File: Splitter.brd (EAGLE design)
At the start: 37.8 x 68.5 mm, 46 parts

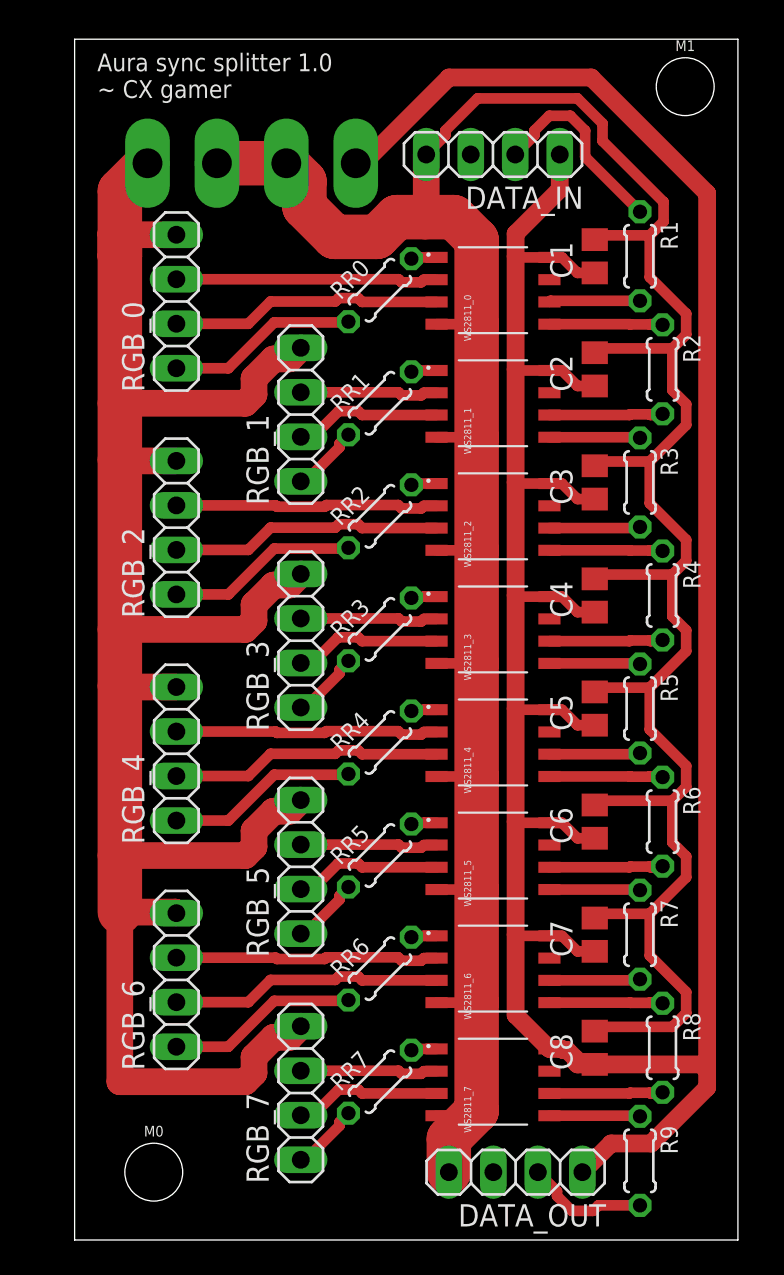
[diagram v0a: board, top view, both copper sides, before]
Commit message: More documentation and upgraded the board to version 1.1
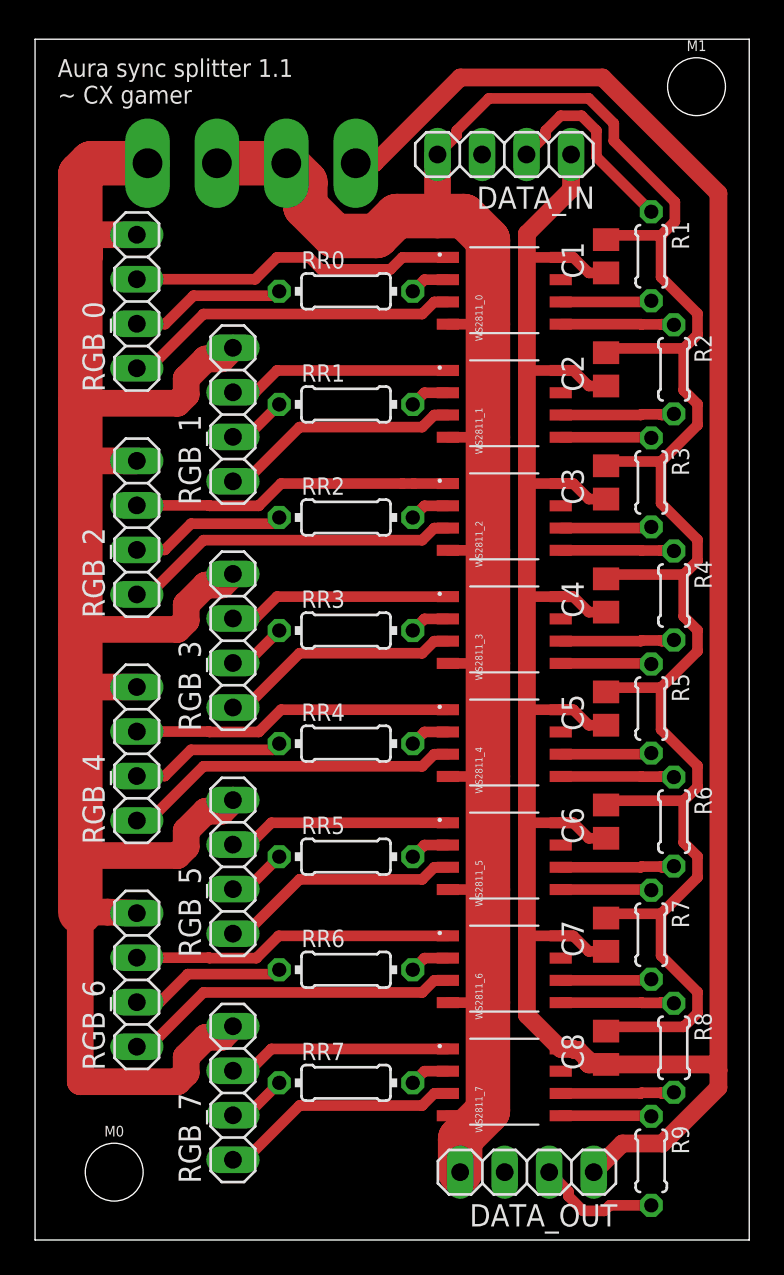
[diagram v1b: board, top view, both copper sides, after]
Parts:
- RR0, RR1, RR2, RR3, RR4, RR5, RR6, RR7: value 30 -> (none); device resistor:0204/5 -> eagle-ltspice:0204/7
- moved RGB_1 3.87 mm to (12.9, 97.4)
- moved RGB_3 3.87 mm to (12.9, 84.5)
- moved RGB_5 3.87 mm to (12.9, 71.6)
- moved RGB_7 3.87 mm to (12.9, 58.7)
- moved RGB_0 2.26 mm to (7.42, 103.9)
- moved RGB_2 2.26 mm to (7.42, 91.0)
- moved RGB_4 2.26 mm to (7.42, 78.1)
- moved RGB_6 2.26 mm to (7.42, 65.2)
- moved M0 2.26 mm to (6.13, 54.2)
- moved RR3 1.94 mm to (19.4, 85.1), turned to 0 degrees
- moved RR4 1.94 mm to (19.4, 78.6), turned to 0 degrees
- moved RR5 1.94 mm to (19.4, 72.2), turned to 0 degrees
- moved RR6 1.94 mm to (19.4, 65.7), turned to 0 degrees
- moved RR0 1.94 mm to (19.4, 104.5), turned to 0 degrees
- moved RR1 1.94 mm to (19.4, 98.0), turned to 0 degrees
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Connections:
- net N$2 renamed S$4
- removed net N$1: RR0.2, WS2811_0.OUTR
- removed net N$11: RR2.2, WS2811_2.OUTR
- removed net N$15: RR3.2, WS2811_3.OUTR
- removed net N$17: RR4.2, WS2811_4.OUTR
- removed net N$19: RR5.2, WS2811_5.OUTR
- removed net N$20: RR6.2, WS2811_6.OUTR
- removed net N$21: RR7.2, WS2811_7.OUTR
- removed net N$24: RGB_5.1, RR5.1
- removed net N$25: RGB_7.2, WS2811_7.OUTB
- removed net N$7: RR1.2, WS2811_1.OUTR
- new net B7: RGB_7.1, WS2811_7.OUTB
- new net R5: RGB_5.2, RR5.1
- new net S$10: RR4.2, WS2811_4.OUTG
- new net S$11: RR5.2, WS2811_5.OUTG
- new net S$13: RR6.2, WS2811_6.OUTG
- new net S$14: RR7.2, WS2811_7.OUTG
- new net S$5: RR0.2, WS2811_0.OUTG
- new net S$6: RR2.2, WS2811_2.OUTG
- new net S$7: RR3.2, WS2811_3.OUTG
- new net S$9: RR1.2, WS2811_1.OUTG
- net B0: now also RGB_0.1; no longer RGB_0.2
- net B1: now also RGB_1.1; no longer RGB_1.2
- net B2: now also RGB_2.1; no longer RGB_2.2
- net B3: now also RGB_3.1; no longer RGB_3.2
- net B4: now also RGB_4.1; no longer RGB_4.2
- net B5: now also RGB_5.1; no longer RGB_5.2
- net B6: now also RGB_6.1; no longer RGB_6.2
- net G0: now also WS2811_0.OUTR; no longer WS2811_0.OUTG
- net G1: now also WS2811_1.OUTR; no longer WS2811_1.OUTG
- net G2: now also WS2811_2.OUTR; no longer WS2811_2.OUTG
- net G3: now also WS2811_3.OUTR; no longer WS2811_3.OUTG
- net G4: now also WS2811_4.OUTR; no longer WS2811_4.OUTG
- net G5: now also WS2811_5.OUTR; no longer WS2811_5.OUTG
- net G6: now also WS2811_6.OUTR; no longer WS2811_6.OUTG
- net G7: now also WS2811_7.OUTR; no longer WS2811_7.OUTG
- net R0: now also RGB_0.2; no longer RGB_0.1
- net R1: now also RGB_1.2; no longer RGB_1.1
- net R2: now also RGB_2.2; no longer RGB_2.1
- net R3: now also RGB_3.2; no longer RGB_3.1
- net R4: now also RGB_4.2; no longer RGB_4.1
- net R6: now also RGB_6.2; no longer RGB_6.1
- net R7: now also RGB_7.2; no longer RGB_7.1
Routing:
- net B7: track 0.00 -> 13.8 mm
- net N$25: track 8.46 -> 0.00 mm
- net B1: track 8.45 -> 13.9 mm
- net B5: track 8.46 -> 13.8 mm
- net B3: track 8.46 -> 13.8 mm
- net G3: track 7.88 -> 12.8 mm
- net G7: track 7.88 -> 12.8 mm
- net G1: track 7.88 -> 12.8 mm
- net G5: track 7.88 -> 12.8 mm
- net N$24: track 3.94 -> 0.00 mm
- net G0: track 15.0 -> 18.8 mm
- net B6: track 15.5 -> 19.4 mm
- net B4: track 15.5 -> 19.3 mm
- net B0: track 15.5 -> 19.3 mm
- net B2: track 15.5 -> 19.3 mm
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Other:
- board size 37.8 x 68.5 mm -> 40.7 x 68.5 mm
- board text added: "Aura sync splitter 1.1 ~ CX gamer"
- board text removed: "Aura sync splitter 1.0 ~ CX gamer"
